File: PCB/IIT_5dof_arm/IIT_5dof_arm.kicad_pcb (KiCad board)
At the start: 2 copper layers, 100 x 100 mm, 97 parts, among them J1 Barrel_Jack_Switch, J14 Conn_02x13_Top_Bottom, J2 I2C 5V, J3 I2C 3V, J4 I2C Display, J5 Jumper_Disp_Vcc, J6 Jumper_Disp_SDA, J7 Jumper_Disp_SCL, Q1 2N7000, Q2 2N7000, SW1 SW_MAIN, SW10 SW_Push, SW11 SW_Push, SW12 SW_Push, SW13 SW_Push, SW14 SW_Push, SW15 SW_MOT, SW2 SW_Push, SW3 RotaryEncoder_Switch, SW4 SW_Push, SW5 SW_Push, SW6 SW_Push, SW7 SW_Push, SW8 SW_Push, SW9 SW_Push, U5 XL8574T, U6 XL8574T, U7 XL8574T

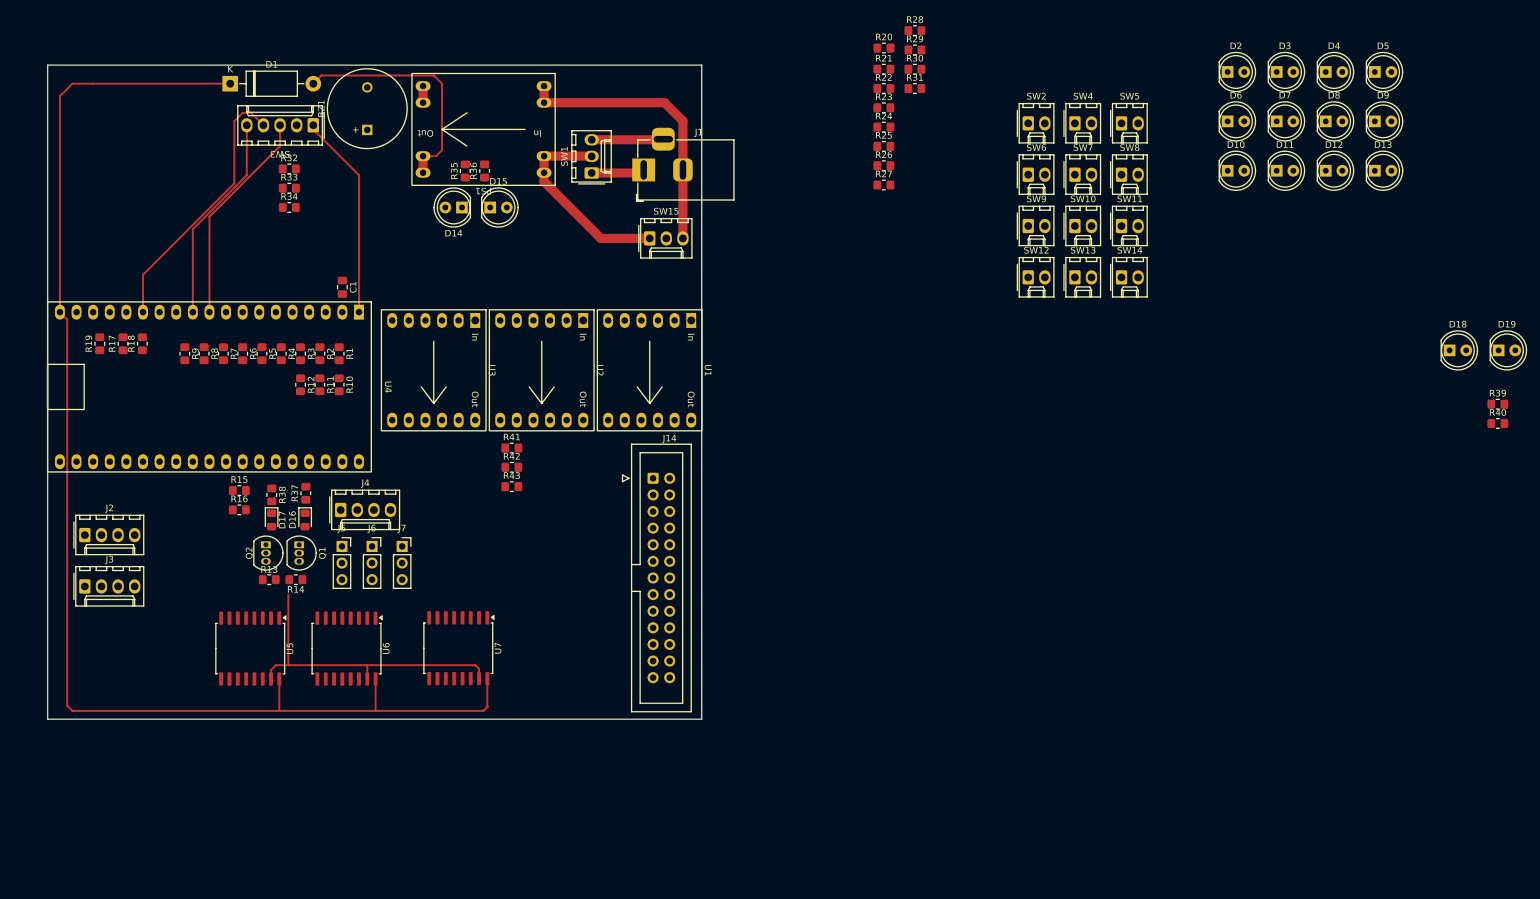
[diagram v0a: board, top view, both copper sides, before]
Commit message: create separate project for IO board
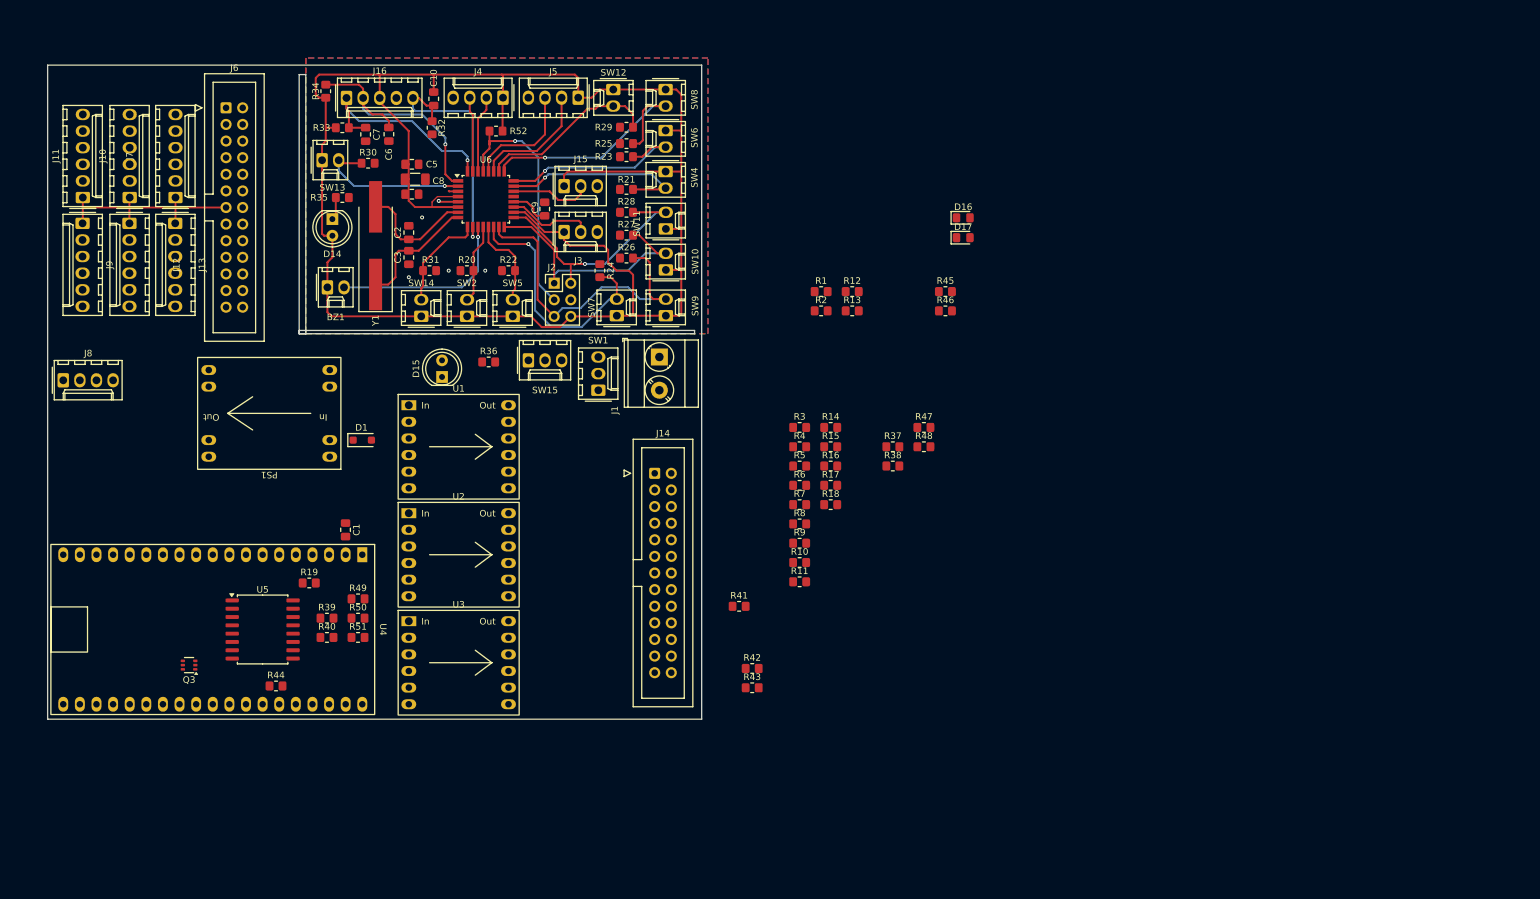
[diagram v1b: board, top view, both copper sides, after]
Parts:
- removed D10, D11, D12, D13, D18, D19, D2, D3, D4, D5, D6, D7, D8, D9: LED, LED_THT:LED_D5.0mm
- removed Q1, Q2: 2N7000, Package_TO_SOT_THT:TO-92_Inline
- removed SW3: RotaryEncoder_Switch, IIT_5dof_arm:Molex_for_encoder_1x05_P2.54mm_Vertical
- removed U7: XL8574T, Package_SO:SOIC-16W_7.5x10.3mm_P1.27mm
- added C10: 100nF, Capacitor_SMD:C_0805_2012Metric_Pad1.18x1.45mm_HandSolder, F.Cu at (113.0, 32.2)
- added C2: 22pF, Capacitor_SMD:C_0805_2012Metric_Pad1.18x1.45mm_HandSolder, F.Cu at (109.2, 52.6)
- added C3: 22pF, Capacitor_SMD:C_0805_2012Metric_Pad1.18x1.45mm_HandSolder, F.Cu at (109.2, 56.4)
- added C4: 1uF, Capacitor_SMD:C_0805_2012Metric_Pad1.18x1.45mm_HandSolder, F.Cu at (109.7, 46.7)
- added C5: 1uF, Capacitor_SMD:C_0805_2012Metric_Pad1.18x1.45mm_HandSolder, F.Cu at (109.7, 42.2)
- added C6: 100nF, Capacitor_SMD:C_0805_2012Metric_Pad1.18x1.45mm_HandSolder, F.Cu at (106.2, 37.6)
- added C7: 100nF, Capacitor_SMD:C_0805_2012Metric_Pad1.18x1.45mm_HandSolder, F.Cu at (102.6, 37.6)
- added C8: 4.7uF, Capacitor_SMD:C_1206_3216Metric_Pad1.33x1.80mm_HandSolder, F.Cu at (110.2, 44.5)
- added C9: 100nF, Capacitor_SMD:C_0805_2012Metric_Pad1.18x1.45mm_HandSolder, F.Cu at (130.0, 49.0)
- added J10: Conn_01x06, Connector_Molex:Molex_KK-254_AE-6410-06A_1x06_P2.54mm_Vertical, F.Cu at (66.5, 47.2)
- added J11: Conn_01x06, Connector_Molex:Molex_KK-254_AE-6410-06A_1x06_P2.54mm_Vertical, F.Cu at (59.4, 47.2)
- added J12: Conn_01x06, Connector_Molex:Molex_KK-254_AE-6410-06A_1x06_P2.54mm_Vertical, F.Cu at (66.5, 51.2)
- added J13: Conn_01x06, Connector_Molex:Molex_KK-254_AE-6410-06A_1x06_P2.54mm_Vertical, F.Cu at (73.5, 51.2)
- added J15: Conn_01x03, Connector_Molex:Molex_KK-254_AE-6410-03A_1x03_P2.54mm_Vertical, F.Cu at (133.0, 45.5)
- added J16: Conn_01x05, Connector_Molex:Molex_KK-254_AE-6410-05A_1x05_P2.54mm_Vertical, F.Cu at (99.7, 32.0)
- added J8: Conn_01x04, Connector_Molex:Molex_KK-254_AE-6410-04A_1x04_P2.54mm_Vertical, F.Cu at (56.4, 75.2)
- added J9: Conn_01x06, Connector_Molex:Molex_KK-254_AE-6410-06A_1x06_P2.54mm_Vertical, F.Cu at (59.3, 51.2)
- added Q3: FDG6335N, Package_TO_SOT_SMD:SOT-363_SC-70-6, F.Cu at (75.6, 118.7)
- added R44: 390, Resistor_SMD:R_0805_2012Metric_Pad1.20x1.40mm_HandSolder, F.Cu at (88.9, 121.9)
- added R45: 390, Resistor_SMD:R_0805_2012Metric_Pad1.20x1.40mm_HandSolder, F.Cu at (191.3, 61.6)
- added R46: 180, Resistor_SMD:R_0805_2012Metric_Pad1.20x1.40mm_HandSolder, F.Cu at (191.3, 64.6)
- added R47: 180, Resistor_SMD:R_0805_2012Metric_Pad1.20x1.40mm_HandSolder, F.Cu at (188.0, 82.4)
- added R48: 180, Resistor_SMD:R_0805_2012Metric_Pad1.20x1.40mm_HandSolder, F.Cu at (188.0, 85.3)
- added R49: 390, Resistor_SMD:R_0805_2012Metric_Pad1.20x1.40mm_HandSolder, F.Cu at (101.5, 108.6)
- added R50: 390, Resistor_SMD:R_0805_2012Metric_Pad1.20x1.40mm_HandSolder, F.Cu at (101.5, 111.5)
- added R51: 390, Resistor_SMD:R_0805_2012Metric_Pad1.20x1.40mm_HandSolder, F.Cu at (101.5, 114.5)
- added R52: 10k, Resistor_SMD:R_0805_2012Metric_Pad1.20x1.40mm_HandSolder, F.Cu at (122.6, 37.1)
- added Y1: 16MHz, Crystal:Crystal_SMD_HC49-SD_HandSoldering, F.Cu at (104.1, 54.6)
- BZ1: footprint Buzzer_Beeper:MagneticBuzzer_ProSignal_ABT-410-RC -> Connector_Molex:Molex_KK-254_AE-6410-02A_1x02_P2.54mm_Vertical
- D1: value D -> D_Schottky; footprint Diode_THT:D_DO-15_P12.70mm_Horizontal -> Diode_SMD:D_SOD-123F
- J1: value Barrel_Jack_Switch -> Screw_Terminal_01x02; footprint Connector_BarrelJack:BarrelJack_Horizontal -> TerminalBlock_Phoenix:TerminalBlock_Phoenix_MKDS-3-2-5.08_1x02_P5.08mm_Horizontal
- J2: value I2C 5V -> Conn_02x03_Counter_Clockwise; footprint Connector_Molex:Molex_KK-254_AE-6410-04A_1x04_P2.54mm_Vertical -> Connector_PinHeader_2.54mm:PinHeader_2x03_P2.54mm_Vertical
- J3: value I2C 3V -> Conn_01x03; footprint Connector_Molex:Molex_KK-254_AE-6410-04A_1x04_P2.54mm_Vertical -> Connector_Molex:Molex_KK-254_AE-6410-03A_1x03_P2.54mm_Vertical
- J4: value I2C Display -> Conn_01x04
- J5: value Jumper_Disp_Vcc -> Conn_01x04; footprint Connector_PinSocket_2.54mm:PinSocket_1x03_P2.54mm_Vertical -> Connector_Molex:Molex_KK-254_AE-6410-04A_1x04_P2.54mm_Vertical
- J6: value Jumper_Disp_SDA -> Conn_02x13_Top_Bottom; footprint Connector_PinSocket_2.54mm:PinSocket_1x03_P2.54mm_Vertical -> Connector_IDC:IDC-Header_2x13_P2.54mm_Vertical
- J7: value Jumper_Disp_SCL -> Conn_01x06; footprint Connector_PinSocket_2.54mm:PinSocket_1x03_P2.54mm_Vertical -> Connector_Molex:Molex_KK-254_AE-6410-06A_1x06_P2.54mm_Vertical
- R13, R14, R15, R16: value 2k2 -> 10k
- R18: value 390 -> 180
- R20, R21, R22, R23, R24, R25, R26, R27, R28, R29, R30, R31, R35, R37, R38: value 10k -> 220
- R36: value 30k -> 590
- R39: value 10k -> 180
- R40: value 10k -> 390
- U6: value XL8574T -> ATmega328P-A; footprint Package_SO:SOIC-16W_7.5x10.3mm_P1.27mm -> Package_QFP:TQFP-32_7x7mm_P0.8mm
- moved R39 182.0 mm to (96.7, 111.5)
- moved R40 182.0 mm to (96.7, 114.5)
- moved SW13 116.5 mm to (96.0, 41.5)
- moved D17 114.2 mm to (194.0, 53.4), turned to 0 degrees
- moved D16 110.7 mm to (194.0, 50.3), turned to 0 degrees
- moved R17 110.3 mm to (173.7, 91.2), turned to 0 degrees
- moved R18 108.1 mm to (173.7, 94.2), turned to 0 degrees
- moved SW14 107.2 mm to (111.1, 65.4), turned to 90 degrees
- moved R9 98.4 mm to (169.0, 100.1), turned to 0 degrees
- moved R13 98.1 mm to (177.0, 64.6), turned to 0 degrees
- moved SW5 97.6 mm to (125.1, 65.4), turned to 90 degrees
- moved R38 95.1 mm to (183.2, 88.3), turned to 0 degrees
- moved R8 94.7 mm to (169.0, 97.1), turned to 0 degrees
- moved J3 91.1 mm to (133.0, 52.5)
- moved R7 91.1 mm to (169.0, 94.2), turned to 0 degrees
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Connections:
- BZ1 pad 1: Net-(BZ1-+) -> UIPanel_+5V
- BZ1 pad 2: GND -> Net-(BZ1--)
- D1 pad 1: +5V -> Net-(D1-K)
- D14 pad 2: +5V -> UIPanel_+5V
- J1 pad 1: +15V -> GNDPWR
- J1 pad 2: GNDPWR -> +15V
- J2 pad 1: +5V -> /UIPanel_BUTT5A__UIPanel_Prog_MISO
- J2 pad 2: /SDA_5v -> /UIPanel_BUTT6A__UIPanel_Prog_SCK
- J2 pad 3: /SCL_5v -> /UIPanel_reset
- J2 pad 4: GND -> UIPanel_GND
- J3 pad 1: +3V3 -> UIPanel_+5V
- J3 pad 2: /SDA_3v3 -> /UIPanel_ADC1
- J3 pad 3: /SCL_3v3 -> UIPanel_GND
- J4 pad 1: /Disp_Vcc -> UIPanel_+5V
- J4 pad 2: /Disp_SDA -> /UIPanel_RX
- J4 pad 3: /Disp_SCL -> /UIPanel_TX
- J4 pad 4: GND -> UIPanel_GND
- J5 pad 1: +3V3 -> UIPanel_+5V
- J5 pad 2: /Disp_Vcc -> /UIPanel_SDA
- J5 pad 3: +5V -> /UIPanel_SCL
- J6 pad 1: /SDA_3v3 -> OutPanel_GND
- J6 pad 2: /Disp_SDA -> /OutPanel_Mot1_OUT1
- J6 pad 3: /SDA_5v -> /OutPanel_Mot1_OUT2
- J7 pad 1: /SCL_3v3 -> OutPanel+5V
- J7 pad 2: /Disp_SCL -> /OutPanel_Mot1_OUT1
- J7 pad 3: /SCL_5v -> /OutPanel_Mot1_OUT2
- PS1 pad 1: Net-(PS1-Vin) -> Net-(D1-K)
- PS1 pad 4: Net-(D1-A) -> +5V
- R13 pad 2: /SDA_5v -> /UI_RX_5v
- R14 pad 2: /SCL_5v -> /UI_TX_5v
- R15 pad 2: /SDA_3v3 -> /UI_RX_3v3
- R16 pad 2: /SCL_3v3 -> /UI_TX_3v3
- R17 pad 1: /extender_INT_5v -> /Mot1_LIMIT_IN
- R17 pad 2: /extender_INT -> /Mot1_LIMIT
- R18 pad 1: GND -> /Mot2_LIMIT_IN
- R18 pad 2: /extender_INT -> /Mot2_LIMIT
- R19 pad 1: /extender_INT_5v -> /extender_INT
- R19 pad 2: +5V -> +3V3
- R20 pad 1: /Mot1_BUTT_A -> UIPanel_GND
- R20 pad 2: GND -> /UIPanel_BUTT1A
- R21 pad 1: /Mot1_BUTT_B -> /UIPanel_BUTT1B
- R21 pad 2: GND -> UIPanel_GND
- R22 pad 1: /Mot2_BUTT_A -> UIPanel_GND
- R22 pad 2: GND -> /UIPanel_BUTT2A
- R23 pad 1: /Mot2_BUTT_B -> /UIPanel_BUTT2B
- R23 pad 2: GND -> UIPanel_GND
- R24 pad 1: /Mot3_BUTT_A -> UIPanel_GND
- R24 pad 2: GND -> /UIPanel_BUTT3A
- R25 pad 1: /Mot3_BUTT_B -> /UIPanel_BUTT3B
- R25 pad 2: GND -> UIPanel_GND
- R26 pad 1: /Mot4_BUTT_A -> UIPanel_GND
- R26 pad 2: GND -> /UIPanel_BUTT4A__UIPanel_Prog_MOSI
- R27 pad 1: /Mot5_BUTT_A -> UIPanel_GND
- R27 pad 2: GND -> /UIPanel_BUTT5A__UIPanel_Prog_MISO
- R28 pad 1: /Mot6_BUTT_A -> UIPanel_GND
- R28 pad 2: GND -> /UIPanel_BUTT6A__UIPanel_Prog_SCK
- R29 pad 1: /Mot4_BUTT_B -> /UIPanel_BUTT4B
- R29 pad 2: GND -> UIPanel_GND
- R30 pad 1: /Mot5_BUTT_B -> /UIPanel_BUTT5B
- R30 pad 2: GND -> UIPanel_GND
- R31 pad 1: /Mot6_BUTT_B -> /UIPanel_BUTT6B
- R31 pad 2: GND -> UIPanel_GND
- R32 pad 1: GND -> /UIPanel_Enc_BUTT
- R32 pad 2: /UI_Enc_BUTT -> UIPanel_GND
- R33 pad 1: /UI_Enc_A -> /UIPanel_Enc_A
- R33 pad 2: +3V3 -> UIPanel_+5V
- R34 pad 1: /UI_Enc_B -> /UIPanel_Enc_B
- R34 pad 2: +3V3 -> UIPanel_+5V
- R35 pad 2: GND -> UIPanel_GND
- R37 pad 2: /SCL_3v3 -> /UI_TX_3v3
- R38 pad 2: /SDA_3v3 -> /UI_RX_3v3
- R39 pad 1: Net-(D18-K) -> /Mot3_LIMIT_IN
- R39 pad 2: /Reserved_LED1 -> /Mot3_LIMIT
- R40 pad 1: Net-(D19-K) -> GND
- R40 pad 2: /Reserved_LED2 -> /Mot1_LIMIT
- SW1 pad 2: Net-(PS1-Vin) -> Net-(D1-A)
- SW1 pad 3: Net-(SW1-C) -> GNDPWR
- SW10 pad 1: Net-(D9-K) -> UIPanel_+5V
- SW10 pad 2: /Mot5_BUTT_A -> /UIPanel_BUTT5A__UIPanel_Prog_MISO
- SW11 pad 1: Net-(D10-K) -> UIPanel_+5V
- SW11 pad 2: /Mot6_BUTT_A -> /UIPanel_BUTT6A__UIPanel_Prog_SCK
- SW12 pad 1: Net-(D11-K) -> UIPanel_+5V
- SW12 pad 2: /Mot4_BUTT_B -> /UIPanel_BUTT4B
- SW13 pad 1: Net-(D12-K) -> UIPanel_+5V
- SW13 pad 2: /Mot5_BUTT_B -> /UIPanel_BUTT5B
- SW14 pad 1: Net-(D13-K) -> UIPanel_+5V
- SW14 pad 2: /Mot6_BUTT_B -> /UIPanel_BUTT6B
- SW15 pad 1: Net-(PS1-Vin) -> Net-(D1-A)
- SW2 pad 1: Net-(D2-K) -> UIPanel_+5V
- SW2 pad 2: /Mot1_BUTT_A -> /UIPanel_BUTT1A
- SW4 pad 1: Net-(D3-K) -> UIPanel_+5V
- SW4 pad 2: /Mot1_BUTT_B -> /UIPanel_BUTT1B
- SW5 pad 1: Net-(D4-K) -> UIPanel_+5V
- SW5 pad 2: /Mot2_BUTT_A -> /UIPanel_BUTT2A
- SW6 pad 1: Net-(D5-K) -> UIPanel_+5V
- SW6 pad 2: /Mot2_BUTT_B -> /UIPanel_BUTT2B
- SW7 pad 1: Net-(D6-K) -> UIPanel_+5V
- SW7 pad 2: /Mot3_BUTT_A -> /UIPanel_BUTT3A
- SW8 pad 1: Net-(D7-K) -> UIPanel_+5V
- SW8 pad 2: /Mot3_BUTT_B -> /UIPanel_BUTT3B
- SW9 pad 1: Net-(D8-K) -> UIPanel_+5V
- SW9 pad 2: /Mot4_BUTT_A -> /UIPanel_BUTT4A__UIPanel_Prog_MOSI
- U4 pad 10: /UI_Enc_A -> /mot4_B
- U4 pad 11: /UI_Enc_B -> /mot3_A
- U4 pad 27: /mot3_A -> /UI_RX_3v3
- U4 pad 28: /mot4_B -> /UI_TX_3v3
- U4 pad 9: Net-(BZ1-+) -> /~{Fault}_12
- U5 pad 10: /Mot6_LIMIT_IN -> /Mot6_LIMIT
- U5 pad 11: /Mot1_BUTT_A -> /~{Fault}_34
- U5 pad 12: /Mot1_BUTT_B -> /~{Fault}_56
- U5 pad 13: /extender_INT_5v -> /extender_INT
- U5 pad 14: /SCL_5v -> /SCL_3v3
- U5 pad 15: /SDA_5v -> /SDA_3v3
- U5 pad 16: +5V -> +3V3
- U5 pad 4: /Mot1_LIMIT_IN -> /Mot1_LIMIT
- U5 pad 5: /Mot2_LIMIT_IN -> /Mot2_LIMIT
- U5 pad 6: /Mot3_LIMIT_IN -> /Mot3_LIMIT
- U5 pad 7: /Mot4_LIMIT_IN -> /Mot4_LIMIT
- U5 pad 9: /Mot5_LIMIT_IN -> /Mot5_LIMIT
- U6 pad 1: +5V -> /UIPanel_Enc_B
- U6 pad 10: /Mot4_BUTT_B -> /UIPanel_Enc_BUTT
- U6 pad 11: /Mot5_BUTT_A -> Net-(BZ1--)
- U6 pad 12: /Mot5_BUTT_B -> /UIPanel_BUTT1A
- U6 pad 13: /extender_INT_5v -> /UIPanel_BUTT2A
- U6 pad 14: /SCL_5v -> /UIPanel_BUTT3A
- U6 pad 15: /SDA_5v -> /UIPanel_BUTT4A__UIPanel_Prog_MOSI
- U6 pad 16: +5V -> /UIPanel_BUTT5A__UIPanel_Prog_MISO
- U6 pad 2: GND -> /UIPanel_BUTT5B
- U6 pad 3: GND -> UIPanel_GND
- U6 pad 4: /Mot2_BUTT_A -> UIPanel_+5V
- U6 pad 5: /Mot2_BUTT_B -> UIPanel_GND
- U6 pad 6: /Mot3_BUTT_A -> UIPanel_+5V
- U6 pad 7: /Mot3_BUTT_B -> /XTAL1
- U6 pad 8: GND -> /XTAL2
- U6 pad 9: /Mot4_BUTT_A -> /UIPanel_BUTT6B
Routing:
- net UIPanel_+5V: track 0.00 -> 293.0 mm
- net +5V: track 199.5 -> 0.00 mm
- net /UIPanel_BUTT4A__UIPanel_Prog_MOSI: track 0.00 -> 50.2 mm
- net /SDA_5v: track 48.1 -> 0.00 mm
- net GND: track 43.3 -> 0.00 mm
- net GNDPWR: track 42.9 -> 0.00 mm
- net /UIPanel_BUTT5A__UIPanel_Prog_MISO: track 0.00 -> 40.1 mm
- net /UIPanel_BUTT3B: track 0.00 -> 39.4 mm, vias 0 -> 1
- net /UIPanel_BUTT3A: track 0.00 -> 38.8 mm, vias 0 -> 1
- net /UIPanel_Enc_B: track 0.00 -> 38.4 mm, vias 0 -> 1
- net /UIPanel_reset: track 0.00 -> 38.3 mm, vias 0 -> 1
- net /UIPanel_BUTT6A__UIPanel_Prog_SCK: track 0.00 -> 38.2 mm, vias 0 -> 1
- net /UIPanel_Enc_BUTT: track 0.00 -> 37.5 mm, vias 0 -> 1
- net Net-(D1-A): track 37.1 -> 0.00 mm
- net OutPanel+5V: track 0.00 -> 33.8 mm
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- added copper zone on B.Cu, net UIPanel_GND
- added copper zone on F.Cu, net UIPanel_GND
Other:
- outline, holes or cut-outs redrawn

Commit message: Control board layout
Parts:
- removed BZ1: Buzzer, Connector_Molex:Molex_KK-254_AE-6410-02A_1x02_P2.54mm_Vertical
- removed C10, C6, C7, C9: 100nF, Capacitor_SMD:C_0805_2012Metric_Pad1.18x1.45mm_HandSolder
- removed C2, C3: 22pF, Capacitor_SMD:C_0805_2012Metric_Pad1.18x1.45mm_HandSolder
- removed C4, C5: 1uF, Capacitor_SMD:C_0805_2012Metric_Pad1.18x1.45mm_HandSolder
- removed C8: 4.7uF, Capacitor_SMD:C_1206_3216Metric_Pad1.33x1.80mm_HandSolder
- removed D14: LED, LED_THT:LED_D5.0mm
- removed J10, J11, J12, J13, J7, J9: Conn_01x06, Connector_Molex:Molex_KK-254_AE-6410-06A_1x06_P2.54mm_Vertical
- removed J15, J3: Conn_01x03, Connector_Molex:Molex_KK-254_AE-6410-03A_1x03_P2.54mm_Vertical
- removed J16: Conn_01x05, Connector_Molex:Molex_KK-254_AE-6410-05A_1x05_P2.54mm_Vertical
- removed J2: Conn_02x03_Counter_Clockwise, Connector_PinHeader_2.54mm:PinHeader_2x03_P2.54mm_Vertical
- removed J4, J5: Conn_01x04, Connector_Molex:Molex_KK-254_AE-6410-04A_1x04_P2.54mm_Vertical
- removed J6: Conn_02x13_Top_Bottom, Connector_IDC:IDC-Header_2x13_P2.54mm_Vertical
- removed Q3: FDG6335N, Package_TO_SOT_SMD:SOT-363_SC-70-6
- removed R1, R11, R17, R18, R3, R39, R46, R47, R48, R5, R7, R9: 180, Resistor_SMD:R_0805_2012Metric_Pad1.20x1.40mm_HandSolder
- removed R10, R12, R2, R4, R40, R44, R45, R49, R50, R51, R6, R8: 390, Resistor_SMD:R_0805_2012Metric_Pad1.20x1.40mm_HandSolder
- removed R13, R14, R15, R16, R32, R33, R34, R52: 10k, Resistor_SMD:R_0805_2012Metric_Pad1.20x1.40mm_HandSolder
- removed R20, R21, R22, R23, R24, R25, R26, R27, R28, R29, R30, R31, R35: 220, Resistor_SMD:R_0805_2012Metric_Pad1.20x1.40mm_HandSolder
- removed SW10, SW11, SW12, SW13, SW14, SW2, SW4, SW5, SW6, SW7, SW8, SW9: SW_Push, Connector_Molex:Molex_KK-254_AE-6410-02A_1x02_P2.54mm_Vertical
- removed U6: ATmega328P-A, Package_QFP:TQFP-32_7x7mm_P0.8mm
- removed Y1: 16MHz, Crystal:Crystal_SMD_HC49-SD_HandSoldering
- added D19: SMAJ12A, Diode_SMD:D_SMA_Handsoldering, F.Cu at (137.9, 38.5)
- added F1: 30R500UF, Capacitor_THT:C_Rect_L13.5mm_W4.0mm_P10.00mm_FKS3_FKP3_MKS4, F.Cu at (139.8, 30.8)
- added G***: LOGO, IIT_5dof_arm:IIT_logo_15x15mm, F.Cu at (101.4, 109.9)
- added REF**: MountingHole_3.2mm_M3, MountingHole:MountingHole_3.2mm_M3, F.Cu at (87.0, 123.0)
- added REF**: MountingHole_3.2mm_M3, MountingHole:MountingHole_3.2mm_M3, F.Cu at (127.0, 123.0)
- added REF**: MountingHole_3.2mm_M3, MountingHole:MountingHole_3.2mm_M3, F.Cu at (87.0, 31.0)
- added REF**: MountingHole_3.2mm_M3, MountingHole:MountingHole_3.2mm_M3, F.Cu at (150.0, 31.0)
- added U7: SN74LV1T34DBV, Package_TO_SOT_SMD:SOT-23-5_HandSoldering, B.Cu at (89.4, 82.2)
- added U8: SN74LV1T34DBV, Package_TO_SOT_SMD:SOT-23-5_HandSoldering, F.Cu at (85.1, 82.5)
- added U9: 4504, Package_DIP:DIP-16_W7.62mm_Socket_LongPads, F.Cu at (118.7, 88.5)
- R42, R43: moved to B.Cu
- moved D17 108.6 mm to (89.5, 83.0), turned to -90 degrees
- moved D16 104.6 mm to (94.6, 83.0), turned to -90 degrees
- moved R38 94.2 mm to (89.5, 78.6), turned to 90 degrees
- moved R37 88.9 mm to (94.6, 78.5), turned to 90 degrees
- moved R41 64.3 mm to (135.2, 50.3), turned to -90 degrees
- moved U4 59.9 mm to (108.0, 60.7)
- moved C1 53.5 mm to (105.5, 44.8), turned to 0 degrees
- moved D1 49.0 mm to (111.8, 36.3), turned to 180 degrees
- moved SW1 48.1 mm to (123.0, 31.1), turned to 180 degrees
- moved PS1 45.4 mm to (103.9, 37.7)
- moved D15 38.3 mm to (130.2, 39.9), turned to 180 degrees
- moved U1 37.1 mm to (145.2, 61.3), turned to -90 degrees
- moved U5 35.6 mm to (108.5, 85.0), turned to 90 degrees
- moved J8 34.6 mm to (88.4, 88.3), turned to -90 degrees
- moved R36 33.9 mm to (133.9, 40.9), turned to -90 degrees
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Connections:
- J1 pad 2: +15V -> Net-(J1-Pin_2)
- J14 pad 10: /Mot3_LIMIT_IN -> /Mot6_ENC
- J14 pad 11: /Mot3_OUT1 -> /Mot3_LIMIT_IN
- J14 pad 12: /Mot3_OUT2 -> /Mot5_ENC
- J14 pad 13: +5V -> /Mot2_LIMIT_IN
- J14 pad 14: /Mot3_ENC_IN -> /Mot1_OUT1
- J14 pad 15: /Mot4_OUT1 -> /Mot1_LIMIT_IN
- J14 pad 16: /Mot4_OUT2 -> /Mot1_OUT2
- J14 pad 17: /Mot4_ENC_IN -> /Mot4_OUT2
- J14 pad 18: /Mot4_LIMIT_IN -> /Mot2_OUT1
- J14 pad 19: /Mot5_OUT1 -> /Mot4_OUT1
- J14 pad 2: /Mot1_OUT1 -> /Mot2_ENC
- J14 pad 20: /Mot5_OUT2 -> /Mot2_OUT2
- J14 pad 21: /Mot5_ENC_IN -> /Mot3_OUT2
- J14 pad 22: /Mot5_LIMIT_IN -> /Mot5_OUT1
- J14 pad 23: /Mot6_OUT1 -> /Mot3_OUT1
- J14 pad 24: /Mot6_OUT2 -> /Mot5_OUT2
- J14 pad 25: /Mot6_ENC_IN -> /Mot6_OUT2
- J14 pad 26: /Mot6_LIMIT_IN -> /Mot6_OUT1
- J14 pad 3: /Mot1_OUT2 -> +5V
- J14 pad 4: /Mot1_ENC_IN -> /Mot1_ENC
- J14 pad 5: /Mot1_LIMIT_IN -> /Mot4_LIMIT_IN
- J14 pad 6: /Mot2_OUT1 -> /Mot4_ENC
- J14 pad 7: /Mot2_OUT2 -> /Mot5_LIMIT_IN
- J14 pad 8: /Mot2_ENC_IN -> /Mot3_ENC
- J14 pad 9: /Mot2_LIMIT_IN -> /Mot6_LIMIT_IN
- U4 pad 10: /mot4_B -> /mot2_A
- U4 pad 11: /mot3_A -> /mot1_B
- U4 pad 12: /mot2_A -> /mot1_A
- U4 pad 13: /mot6_A -> /~{Fault}_12
- U4 pad 23: /mot2_B -> /mot6_B
- U4 pad 24: /mot1_B -> /mot6_A
- U4 pad 25: /mot1_A -> /mot5_B
- U4 pad 26: /mot3_B -> /mot5_A
- U4 pad 29: /mot4_A -> /mot4_B
- U4 pad 30: /mot5_B -> /mot4_A
- U4 pad 31: /mot5_A -> /mot3_B
- U4 pad 37: /mot6_B -> /mot3_A
- U4 pad 9: /~{Fault}_12 -> /mot2_B
- U5 pad 10: /Mot6_LIMIT -> /Mot5_LIMIT
- U5 pad 11: /~{Fault}_34 -> /Mot4_LIMIT
- U5 pad 12: /~{Fault}_56 -> /Mot3_LIMIT
- U5 pad 4: /Mot1_LIMIT -> /~{Fault}_56
- U5 pad 5: /Mot2_LIMIT -> /~{Fault}_34
- U5 pad 6: /Mot3_LIMIT -> /Mot2_LIMIT
- U5 pad 7: /Mot4_LIMIT -> /Mot1_LIMIT
- U5 pad 9: /Mot5_LIMIT -> /Mot6_LIMIT
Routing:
- net UIPanel_+5V: track 293.0 -> 0.00 mm
- net GNDPWR: track 0.00 -> 162.2 mm
- net +3V3: track 0.00 -> 148.4 mm, vias 0 -> 3
- net VCC: track 0.00 -> 133.3 mm
- net +5V: track 0.00 -> 130.3 mm, vias 0 -> 3
- net /Mot5_ENC: track 0.00 -> 68.8 mm
- net /mot6_B: track 0.00 -> 66.4 mm
- net /Mot6_ENC: track 0.00 -> 65.2 mm
- net /Mot3_ENC: track 0.00 -> 64.1 mm
- net /~{Fault}_12: track 0.00 -> 63.2 mm, vias 0 -> 1
- net /mot6_A: track 0.00 -> 62.8 mm
- net /Mot4_ENC: track 0.00 -> 62.1 mm
- net /Mot1_ENC: track 0.00 -> 59.9 mm
- net /Mot2_ENC: track 0.00 -> 57.4 mm
- net /mot1_A: track 0.00 -> 56.4 mm, vias 0 -> 1
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- added copper zone on B.Cu, net GND
- added copper zone on F.Cu, net GND
- removed copper zone on B.Cu, net UIPanel_GND
- removed copper zone on F.Cu, net UIPanel_GND
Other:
- board size 100 x 100 mm -> 71.1 x 100 mm
- board text added: "+"
- board text added: "+12V"
- board text added: "+5V"
- board text added: "-"
- board text added: "GND"
- board text added: "Kalms&Mürb Teach-robot Custom control panel v1.0 András Izsó"
- board text added: "RX"
- board text added: "TX"
- board text added: "UI Panel connection"

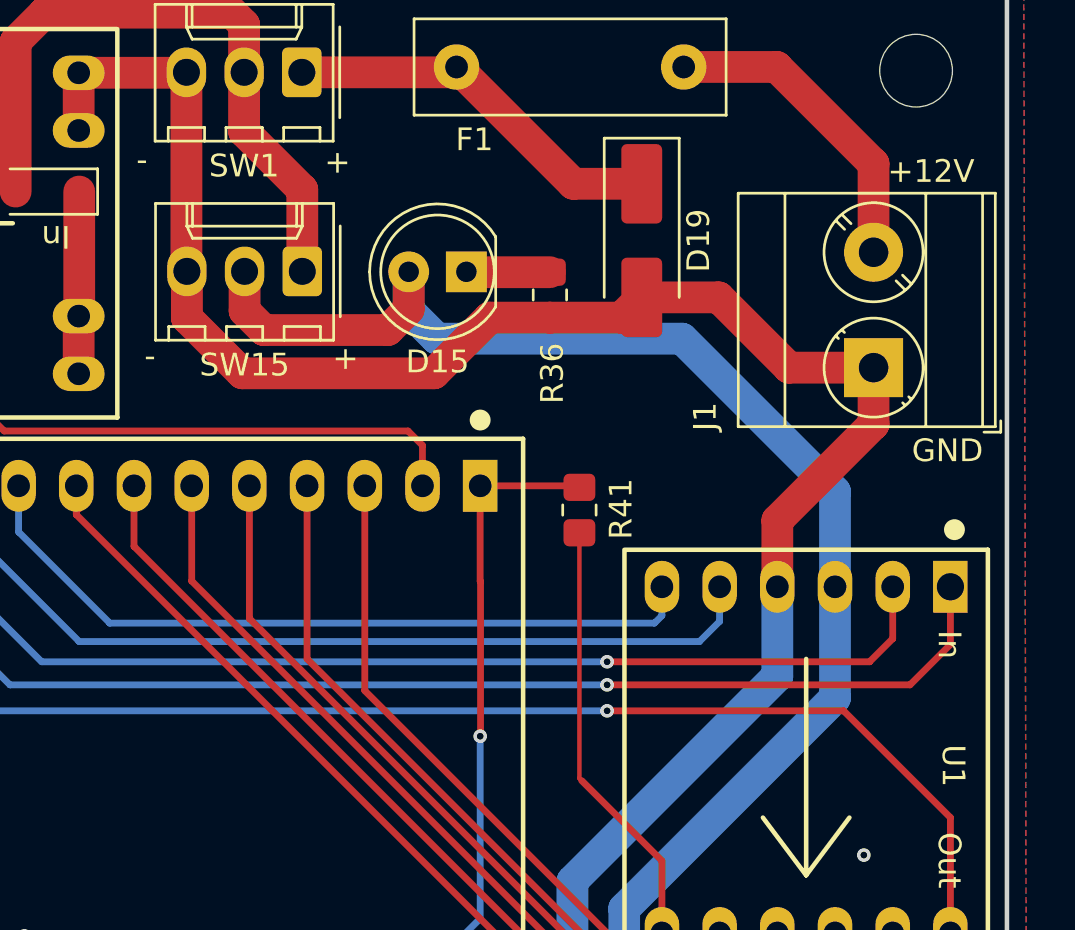
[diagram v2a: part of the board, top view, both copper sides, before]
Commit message: Change motor power LED footprint to connector
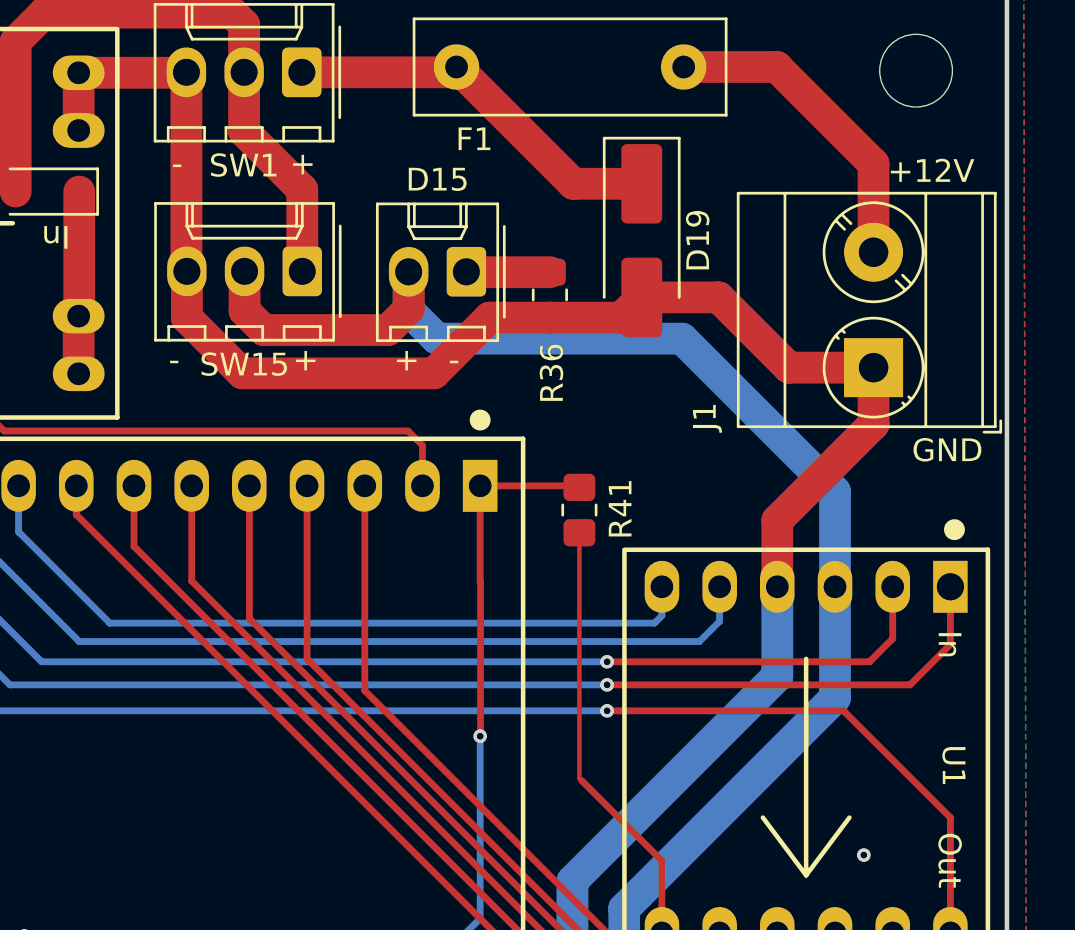
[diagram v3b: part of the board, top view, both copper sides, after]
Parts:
- D15: footprint LED_THT:LED_D5.0mm -> Connector_Molex:Molex_KK-254_AE-6410-02A_1x02_P2.54mm_Vertical
